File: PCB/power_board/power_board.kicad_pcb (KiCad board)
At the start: 2 copper layers, 70 x 70 mm, 57 parts, among them IC10 LSM6DSV16BXTR, IC11 TPS61032PWP, IC7 BQ51013BRHLR, IC8 TPS63000IDRCRQ1, IC9 MAX17048G+T10, J10 Conn_01x15, J11 Conn_01x15, J7 Conn_01x02, J8 UJ20-C-H-G-MSMT-R-4C-P16-TR, J9 QVAR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

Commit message: everything on pcb
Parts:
- C19, C20, C21, C22, C23, C24, C25, C27, C28, C29, C30, C34, C35, C36, D5, D6, D7, L3, L4, Q2, R18, R26, R28, TH4: moved to B.Cu
- moved U2 169.8 mm to (192.4, 78.4)
- moved R21 158.3 mm to (176.4, 78.0)
- moved C32 157.7 mm to (189.5, 85.0)
- moved R19 142.9 mm to (165.0, 83.0)
- moved TH3 142.0 mm to (154.2, 83.0)
- moved R24 142.0 mm to (170.2, 89.0)
- moved R17 140.0 mm to (176.2, 83.0)
- moved R28 134.9 mm to (190.8, 97.0), turned to 180 degrees
- moved R22 132.1 mm to (165.2, 78.0)
- moved R26 125.1 mm to (190.8, 101.0), turned to 180 degrees
- moved R23 123.8 mm to (154.0, 78.0)
- moved C36 123.8 mm to (176.0, 111.0), turned to 180 degrees
- moved R20 121.1 mm to (158.2, 89.0)
- moved C35 118.0 mm to (174.0, 107.0)
- moved L3 113.3 mm to (191.1, 111.0), turned to 180 degrees
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
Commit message: routing done
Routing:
- net GND: track 0.00 -> 393.6 mm, vias 0 -> 7
- net /V_SYS: track 0.00 -> 148.0 mm
- net /Movement/VOUT_3V3: track 0.00 -> 145.4 mm, vias 0 -> 4
- net /CHARGER_SRC: track 0.00 -> 114.6 mm, vias 0 -> 2
- net Net-(IC7-BOOT1): track 0.00 -> 104.9 mm, vias 0 -> 3
- net /TS/CTRL: track 0.00 -> 94.4 mm, vias 0 -> 3
- net /I2C_SCL: track 0.00 -> 92.3 mm, vias 0 -> 1
- net /STEP_UP/OUT+5V: track 0.00 -> 89.3 mm, vias 0 -> 2
- net Net-(IC7-AC2): track 0.00 -> 88.8 mm
- net Net-(D7-A): track 0.00 -> 87.0 mm, vias 0 -> 3
- net /BAT+: track 0.00 -> 81.0 mm, vias 0 -> 1
- net Net-(IC7-~{CHG}): track 0.00 -> 80.3 mm, vias 0 -> 1
- net Net-(D5-A): track 0.00 -> 69.7 mm, vias 0 -> 2
- net Net-(IC7-FOD): track 0.00 -> 68.9 mm, vias 0 -> 1
- net Net-(IC11-SW_1): track 0.00 -> 66.4 mm, vias 0 -> 1
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
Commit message: everything before jlc template
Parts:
- removed J10, J11: Conn_01x15, Connector_PinHeader_2.54mm:PinHeader_1x15_P2.54mm_Vertical
- added J1: Speaker_con, Connector_PinHeader_2.54mm:PinHeader_1x02_P2.54mm_Vertical, F.Cu at (211.0, 78.0)
- added J2: DS1013-40SSIB1-B-0, DS1013-40SSIB1-B-0:DS101340SSIB1B0, F.Cu at (196.5, 65.0)
- moved IC9 45.7 mm to (148.0, 84.8)
- moved U2 35.9 mm to (157.0, 72.0)
- moved IC11 30.9 mm to (184.0, 71.9), turned to 0 degrees
- moved IC10 28.5 mm to (206.2, 78.2)
- moved IC7 24.8 mm to (171.6, 72.0)
- moved C31 18.8 mm to (205.0, 87.0)
- moved C25 9.71 mm to (159.5, 108.0)
- moved S2 8.00 mm to (209.0, 62.0)
- moved C19 7.07 mm to (158.0, 56.0)
- moved Q2 6.98 mm to (149.1, 110.0)
- moved D7 6.40 mm to (189.0, 62.0), turned to -90 degrees
- moved J9 6.08 mm to (206.0, 109.0)
- moved J8 5.31 mm to (160.4, 115.8)
- moved C32 3.61 mm to (186.5, 83.0)
- moved D8 3.10 mm to (168.2, 108.0)
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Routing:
- net Net-(IC7-~{CHG}): track 80.3 -> 0.00 mm, vias 1 -> 0
- net /I2C_SCL: track 92.3 -> 17.2 mm
- net /STEP_UP/OUT+5V: track 89.3 -> 21.4 mm, vias 2 -> 1
- net Net-(S2-COM): track 28.3 -> 87.1 mm, vias 1 -> 0
- net Net-(IC10-AH2/QVAR2): track 7.41 -> 63.6 mm, vias 0 -> 1
- net Net-(IC7-OUT): track 51.6 -> 0.00 mm, vias 2 -> 0
- net /USB_SRC: track 22.5 -> 61.2 mm, vias 1 -> 2
- net Net-(IC7-ILIM): track 52.9 -> 17.3 mm, vias 2 -> 1
- net Net-(IC7-FOD): track 68.9 -> 35.8 mm, vias 1 -> 0
- net /BAT+: track 81.0 -> 113.3 mm
- net Net-(IC7-BOOT2): track 30.4 -> 0.00 mm, vias 1 -> 0
- net Net-(U2-THERM): track 41.6 -> 11.6 mm, vias 0 -> 1
- net Net-(J1-Pin_2): track 0.00 -> 27.7 mm, vias 0 -> 1
- net Net-(IC7-COMM1): track 42.1 -> 15.7 mm
- net Net-(J1-Pin_1): track 0.00 -> 26.3 mm
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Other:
- outline, holes or cut-outs redrawn

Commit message: working on routing
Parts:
- moved C25 2.00 mm to (157.5, 108.0), turned to 0 degrees
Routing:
- net GND: track 391.6 -> 26.5 mm, vias 3 -> 0
- net /Movement/VOUT_3V3: track 133.5 -> 0.00 mm, vias 3 -> 0
- net /V_SYS: track 121.9 -> 0.00 mm, vias 1 -> 0
- net /BAT+: track 113.3 -> 0.00 mm, vias 1 -> 0
- net Net-(IC7-BOOT1): track 110.9 -> 0.00 mm, vias 1 -> 0
- net /CHARGER_SRC: track 103.2 -> 0.00 mm, vias 1 -> 0
- net Net-(S2-COM): track 87.1 -> 0.00 mm
- net Net-(D7-A): track 84.7 -> 0.00 mm, vias 3 -> 0
- net Net-(IC7-AC2): track 75.4 -> 0.00 mm, vias 1 -> 0
- net /USB_D+: track 74.8 -> 0.00 mm, vias 1 -> 0
- net /TS/CTRL: track 74.0 -> 0.00 mm, vias 3 -> 0
- net /USB_D-: track 73.2 -> 0.00 mm, vias 2 -> 0
- net Net-(J7-Pin_1): track 70.2 -> 0.00 mm, vias 1 -> 0
- net /I2C_SDA: track 66.6 -> 0.00 mm, vias 3 -> 0
- net Net-(IC10-AH2/QVAR2): track 63.6 -> 0.00 mm, vias 1 -> 0
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
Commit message: ECR passed
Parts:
- moved J2 54.5 mm to (247.5, 45.8)
- moved AC1 54.2 mm to (237.0, 71.5)
- moved BT2 54.2 mm to (257.0, 81.0)
- moved C19 54.2 mm to (208.8, 37.0)
- moved C20 54.2 mm to (235.3, 39.0)
- moved C21 54.2 mm to (209.3, 46.0)
- moved C22 54.2 mm to (251.8, 35.0)
- moved C23 54.2 mm to (234.8, 46.0)
- moved C24 54.2 mm to (216.8, 38.0)
- moved C25 54.2 mm to (208.3, 89.0)
- moved C26 54.2 mm to (199.8, 59.0)
- moved C27 54.2 mm to (201.3, 46.0)
- moved C28 54.2 mm to (216.3, 46.0)
- moved C29 54.2 mm to (226.3, 46.0)
- moved C30 54.2 mm to (226.3, 38.0)
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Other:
- board size 70 x 70 mm -> 210.8 x 108.4 mm

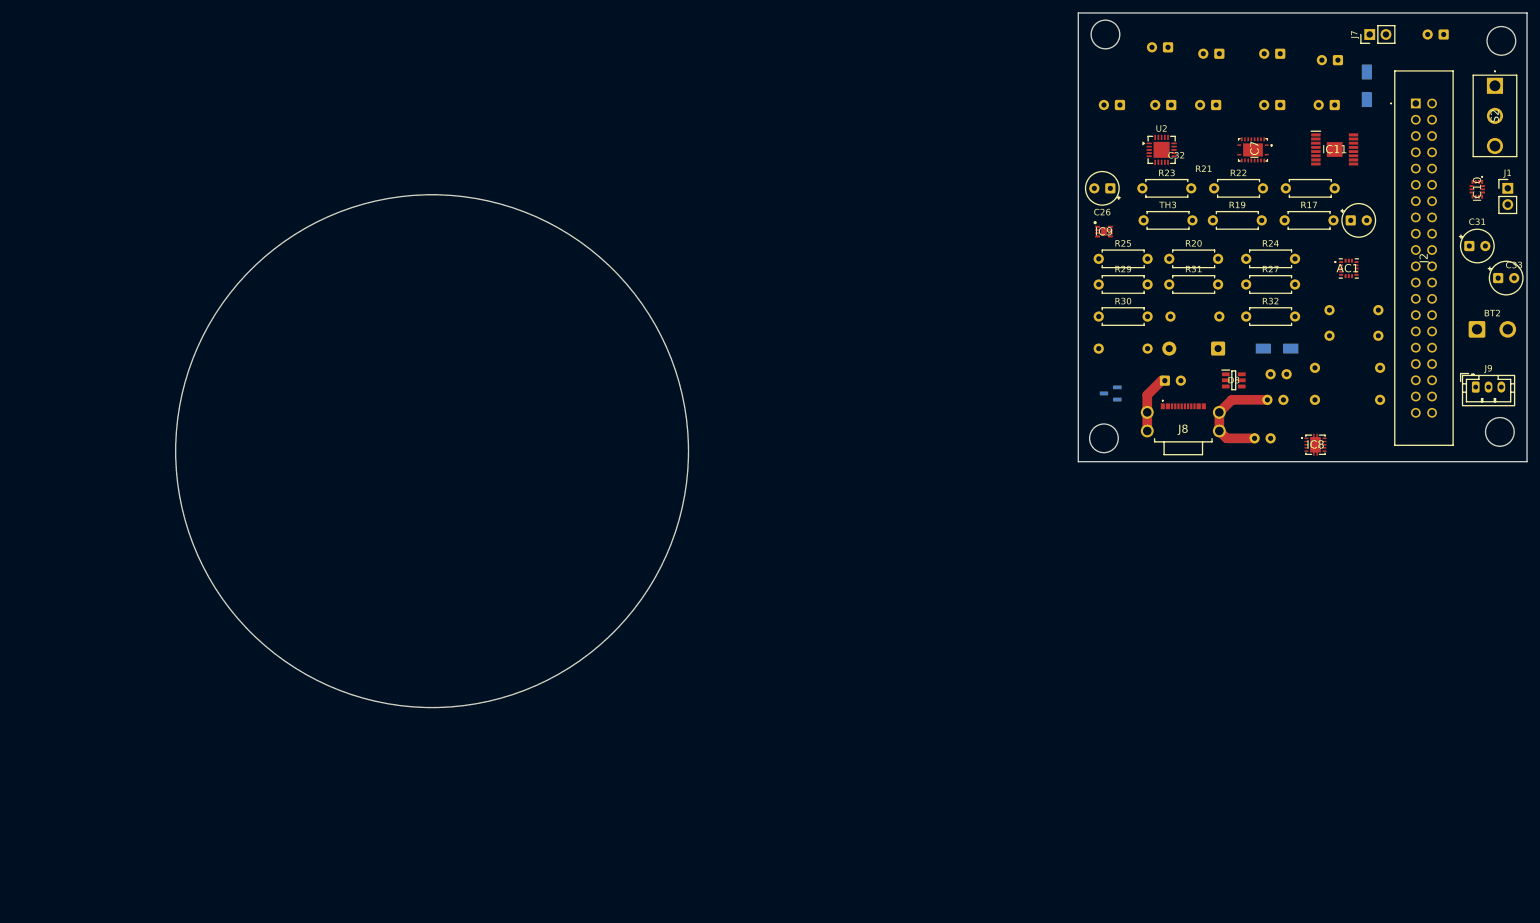
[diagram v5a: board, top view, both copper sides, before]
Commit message: two layers routing done
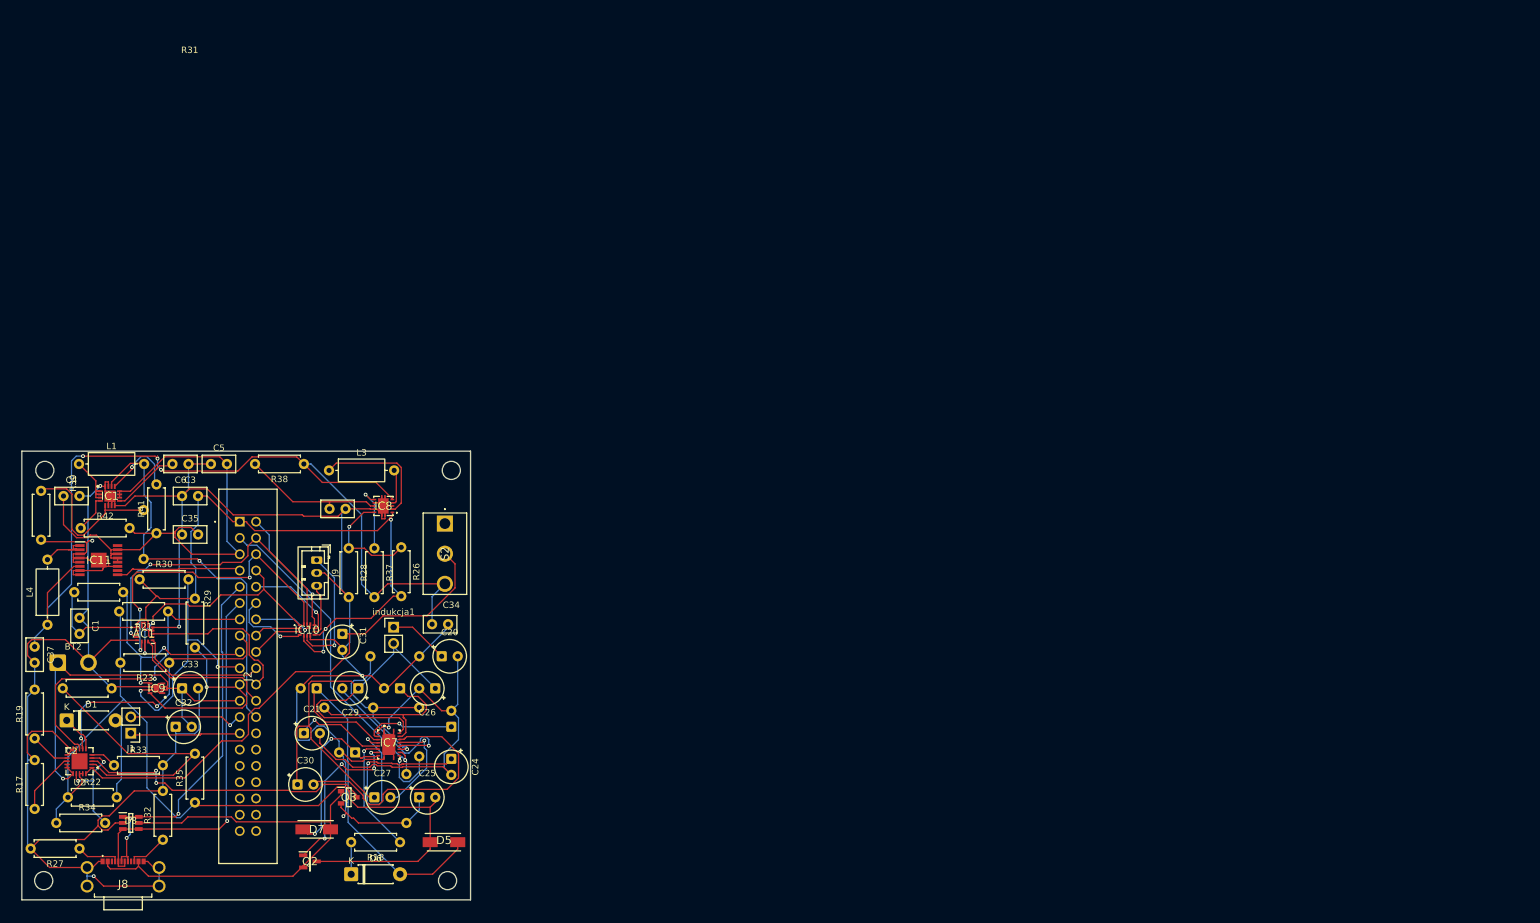
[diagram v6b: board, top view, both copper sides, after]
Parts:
- removed C36: 220µF, Capacitor_THT:C_Disc_D5.0mm_W2.5mm_P2.50mm
- removed J7: Conn_01x02, Connector_PinHeader_2.54mm:PinHeader_1x02_P2.54mm_Vertical
- removed TH3: 10kΩ, Resistor_THT:R_Axial_DIN0207_L6.3mm_D2.5mm_P7.62mm_Horizontal
- added C1: 10μF, Capacitor_THT:C_Disc_D5.0mm_W2.5mm_P2.50mm, F.Cu at (39.0, 126.0)
- added C2: 0.1μF, Capacitor_THT:C_Disc_D5.0mm_W2.5mm_P2.50mm, F.Cu at (78.0, 109.0)
- added C3: 10μF, Capacitor_THT:C_Disc_D5.0mm_W2.5mm_P2.50mm, F.Cu at (55.0, 107.0)
- added C37: 10µF, Capacitor_THT:C_Disc_D5.0mm_W2.5mm_P2.50mm, F.Cu at (32.0, 130.5)
- added C4: 220µF, Capacitor_THT:C_Disc_D5.0mm_W2.5mm_P2.50mm, F.Cu at (36.5, 107.0)
- added C5: 10µF, Capacitor_THT:C_Disc_D5.0mm_W2.5mm_P2.50mm, F.Cu at (59.5, 102.0)
- added C6: 10µF, Capacitor_THT:C_Disc_D5.0mm_W2.5mm_P2.50mm, F.Cu at (56.0, 102.0)
- added D1: LED, Diode_THT:D_DO-41_SOD81_P7.62mm_Horizontal, F.Cu at (37.0, 142.0)
- added IC1: TPS6213013AQRGTTQ1, TPS6213013AQRGTTQ1:QFN50P300X300X100-17N-D, F.Cu at (43.8, 107.0)
- added L1: 2.2µH, Inductor_THT:L_Axial_L7.0mm_D3.3mm_P10.16mm_Horizontal_Fastron_MICC, F.Cu at (38.9, 102.0)
- added Q3: BSS138, BSS138:SOT95P240X120-3N, F.Cu at (81.0, 154.0)
- added R33: 10kΩ, Resistor_THT:R_Axial_DIN0207_L6.3mm_D2.5mm_P7.62mm_Horizontal, F.Cu at (44.4, 149.0)
- added R34: 1kΩ, Resistor_THT:R_Axial_DIN0207_L6.3mm_D2.5mm_P7.62mm_Horizontal, F.Cu at (35.4, 158.0)
- added R35: 330kΩ, Resistor_THT:R_Axial_DIN0207_L6.3mm_D2.5mm_P7.62mm_Horizontal, F.Cu at (57.0, 154.8)
- added R36: 110kΩ, Resistor_THT:R_Axial_DIN0207_L6.3mm_D2.5mm_P7.62mm_Horizontal, F.Cu at (36.4, 137.0)
- added R37: 10kΩ, Resistor_THT:R_Axial_DIN0207_L6.3mm_D2.5mm_P7.62mm_Horizontal, F.Cu at (85.0, 115.2)
- added R38: 100kΩ, Resistor_THT:R_Axial_DIN0207_L6.3mm_D2.5mm_P7.62mm_Horizontal, F.Cu at (74.0, 102.0)
- added R39: 200kΩ, Resistor_THT:R_Axial_DIN0207_L6.3mm_D2.5mm_P7.62mm_Horizontal, F.Cu at (33.0, 106.2)
- added R40: 750kΩ, Resistor_THT:R_Axial_DIN0207_L6.3mm_D2.5mm_P7.62mm_Horizontal, B.Cu at (49.0, 116.8)
- added R41: 10kΩ, Resistor_THT:R_Axial_DIN0207_L6.3mm_D2.5mm_P7.62mm_Horizontal, F.Cu at (51.0, 112.8)
- added R42: 100kΩ, Resistor_THT:R_Axial_DIN0207_L6.3mm_D2.5mm_P7.62mm_Horizontal, F.Cu at (39.2, 112.0)
- added indukcja1: Conn_01x02, Connector_PinHeader_2.54mm:PinHeader_1x02_P2.54mm_Vertical, F.Cu at (88.0, 127.5)
- C20: value C -> C1; moved to F.Cu
- C21, C29: value 10µF -> 22µF; moved to F.Cu
- C24, C25, C27, C30, C34, C35, D5, D6, D7, L3, L4, Q2, R18, R26: moved to F.Cu
- C26: value C -> C2
- C31: value 4.7µF -> 10µF
- R17: value 10kΩ -> 1kΩ
- R19: value 10kΩ -> 100kΩ
- R20, R24, R25: moved to B.Cu
- R21, R22, R23: value 470Ω -> 10Ω
- R28: value 178kΩ -> 180kΩ; moved to F.Cu
- moved J1 231.0 mm to (47.0, 144.0), turned to 180 degrees
- moved BT2 227.4 mm to (35.6, 133.0)
- moved R17 215.5 mm to (32.0, 155.8), turned to 90 degrees
- moved C33 215.1 mm to (55.0, 137.0)
- moved L4 211.7 mm to (34.0, 127.1), turned to 90 degrees
- moved C22 203.4 mm to (82.0, 147.0)
- moved IC11 203.2 mm to (42.0, 117.0)
- moved R22 202.5 mm to (37.2, 154.0)
- moved R27 202.2 mm to (39.0, 162.0), turned to 180 degrees
- moved R19 200.8 mm to (32.0, 144.8), turned to 90 degrees
- moved D7 200.7 mm to (76.0, 159.0), turned to 0 degrees
- moved C32 199.6 mm to (54.0, 143.0)
- moved AC1 196.3 mm to (49.2, 128.5)
- moved IC10 195.1 mm to (74.5, 127.9), turned to 0 degrees
- moved J2 194.7 mm to (64.0, 111.0)
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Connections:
- C19 pad 1: Net-(IC7-OUT) -> Net-(D5-A)
- C19 pad 2: Net-(D5-A) -> GND
- C20 pad 1: Net-(J7-Pin_1) -> Net-(indukcja1-Pin_1)
- C24 pad 1: Net-(IC7-BOOT1) -> Net-(IC7-CLAMP1)
- C26 pad 2: Net-(J7-Pin_1) -> Net-(IC7-AC1)
- IC7 pad 4: Net-(IC7-OUT) -> Net-(D5-A)
- IC7 pad 5: Net-(IC7-BOOT1) -> Net-(IC7-CLAMP1)
- IC7 pad 8: Net-(IC7-BOOT1) -> Net-(IC7-~{AD-EN})
- IC8 pad 6: /V_SYS -> Net-(IC8-EN)
- IC8 pad 8: /V_SYS -> Net-(IC8-VINA)
- J2 pad 26: unconnected-(J2-Pad26) -> /3V8
- Q2 pad 1: Net-(IC7-BOOT1) -> Net-(IC7-~{AD-EN})
- R22 pad 2: Net-(U2-~{PG}) -> Net-(D1-A)
- U2 pad 17: /CHARGER_SRC -> Net-(U2-CE)
- U2 pad 2: /CHARGER_SRC -> Net-(U2-VPCC)
- U2 pad 3: /CHARGER_SRC -> Net-(Q3-D)
- U2 pad 4: /CHARGER_SRC -> Net-(U2-CE)
- U2 pad 6: Net-(U2-~{PG}) -> Net-(D1-K)
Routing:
- net GND: track 26.5 -> 467.7 mm, vias 0 -> 6
- net /V_SYS: track 0.00 -> 146.2 mm, vias 0 -> 3
- net /CHARGER_SRC: track 0.00 -> 135.7 mm
- net /Movement/VOUT_3V3: track 0.00 -> 122.3 mm, vias 0 -> 3
- net /STEP_UP/OUT+5V: track 0.00 -> 85.5 mm
- net Net-(IC7-AC2): track 0.00 -> 84.9 mm
- net Net-(S2-COM): track 0.00 -> 81.6 mm
- net Net-(D7-A): track 0.00 -> 78.8 mm
- net /BAT+: track 0.00 -> 62.2 mm, vias 0 -> 1
- net Net-(IC7-AC1): track 0.00 -> 62.1 mm, vias 0 -> 1
- net /3V8: track 0.00 -> 61.8 mm, vias 0 -> 1
- net Net-(D5-A): track 0.00 -> 61.6 mm
- net /USB_D-: track 0.00 -> 59.6 mm, vias 0 -> 1
- net /USB_D+: track 0.00 -> 58.5 mm, vias 0 -> 3
- net /STAT1: track 0.00 -> 50.7 mm, vias 0 -> 1
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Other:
- board size 210.8 x 108.4 mm -> 70 x 70 mm
- copper layers 2 -> 4

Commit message: own routes with errors done
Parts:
- moved BT2 7.99 mm to (42.2, 137.5), turned to 180 degrees
- moved R30 7.34 mm to (55.7, 119.7), turned to 180 degrees
- moved R31 6.81 mm to (45.0, 121.8), turned to 180 degrees
- moved R36 4.46 mm to (35.2, 132.7)
- moved J1 3.22 mm to (50.0, 145.2)
- moved D1 1.97 mm to (38.9, 142.6)
- moved C1 1.85 mm to (39.0, 127.8), turned to 90 degrees
- moved C24 1.80 mm to (97.1, 149.8), turned to 90 degrees
- moved R39 0.81 mm to (33.4, 105.5)
- moved R20 0.76 mm to (92.7, 140.3)
- moved IC11 0.64 mm to (41.4, 117.0)
- moved L4 0.59 mm to (34.1, 127.7)
- moved R28 0.50 mm to (81.5, 115.1)
- moved IC1 0.50 mm to (43.2, 107.0)
- moved C28 0.45 mm to (89.2, 136.6)
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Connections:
- J2 pad 11: /USB_D- -> unconnected-(J2-Pad11)
- J2 pad 2: /Movement/WCLK -> /3V8
- J2 pad 20: /Movement/ACCEL_INT2 -> /Movement/ACCEL_INT1
- J2 pad 22: /Movement/ACCEL_INT1 -> /Movement/ACCEL_INT2
- J2 pad 26: /3V8 -> /Movement/WCLK
- J2 pad 37: unconnected-(J2-Pad37) -> /USB_D+
- J2 pad 39: unconnected-(J2-Pad39) -> /USB_D-
- J2 pad 6: /Movement/MOSI -> /Movement/MISO
- J2 pad 8: /Movement/MISO -> /Movement/MOSI
- J2 pad 9: /USB_D+ -> unconnected-(J2-Pad9)
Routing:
- net GND: track 467.7 -> 78.6 mm, vias 6 -> 35
- net Net-(IC7-AC2): track 84.9 -> 37.3 mm, vias 0 -> 1
- net Net-(D5-A): track 61.6 -> 24.0 mm
- net /USB_D-: track 59.6 -> 24.1 mm, vias 1 -> 4
- net /USB_D+: track 58.5 -> 28.9 mm, vias 3 -> 2
- net /Movement/VOUT_3V3: track 122.3 -> 149.8 mm, vias 3 -> 2
- net Net-(IC8-L2): track 19.4 -> 0.00 mm
- net Net-(J1-Pin_2): track 18.1 -> 0.00 mm, vias 1 -> 0
- net Net-(IC7-BOOT2): track 41.5 -> 23.7 mm, vias 0 -> 3
- net Net-(D7-A): track 78.8 -> 61.1 mm
- net Net-(J1-Pin_1): track 17.5 -> 0.00 mm
- net Net-(IC7-CLAMP1): track 34.9 -> 18.1 mm, vias 2 -> 0
- net Net-(IC7-AC1): track 62.1 -> 45.5 mm, vias 1 -> 0
- net /Movement/MOSI: track 50.4 -> 37.6 mm
- net Net-(IC7-RECT): track 27.2 -> 14.3 mm, vias 0 -> 1
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- added copper zone on In1.Cu, net GND

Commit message: most errors solved
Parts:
- moved R27 17.5 mm to (55.5, 167.8), turned to 0 degrees
- moved J8 4.27 mm to (43.1, 164.4)
- moved D8 3.20 mm to (49.0, 155.5)
- moved R32 1.83 mm to (53.9, 159.9)
- moved C19 1.54 mm to (76.9, 135.8)
- moved R34 1.06 mm to (34.7, 157.2)
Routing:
- net Net-(IC7-AC2): track 37.3 -> 75.9 mm, vias 1 -> 2
- net Net-(D5-A): track 24.0 -> 58.1 mm, vias 0 -> 3
- net Net-(J8-CC1): track 6.96 -> 28.4 mm
- net Net-(J1-Pin_1): track 0.00 -> 20.7 mm, vias 0 -> 1
- net /FG_ALRT: track 24.1 -> 44.7 mm, vias 0 -> 2
- net Net-(J1-Pin_2): track 0.00 -> 19.9 mm, vias 0 -> 1
- net Net-(IC8-L2): track 0.00 -> 18.6 mm, vias 0 -> 1
- net Net-(IC7-RECT): track 14.3 -> 27.7 mm
- net Net-(D7-A): track 61.1 -> 74.1 mm, vias 0 -> 2
- net /USB_D-: track 24.1 -> 35.6 mm, vias 4 -> 3
- net GND: track 78.6 -> 89.6 mm, vias 35 -> 33
- net Net-(indukcja1-Pin_1): track 0.00 -> 10.1 mm
- net Net-(IC7-FOD): track 20.2 -> 28.4 mm
- net Net-(IC8-L1): track 0.00 -> 7.42 mm, vias 0 -> 1
- net Net-(J8-CC2): track 7.17 -> 11.8 mm
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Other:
- outline, holes or cut-outs redrawn
